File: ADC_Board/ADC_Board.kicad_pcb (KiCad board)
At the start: 2 copper layers, 93 x 57.7 mm, 60 parts, among them IC1 UCC12040DVE, IC2 ADS131M04QPWRQ1, IC7 ISO7762FDWR, J1 Conn_01x01_Pin, J2 Conn_01x01_Pin, J3 Conn_01x08_Pin, J4 Conn_01x01_Pin, J5 Conn_01x01_Pin, J6 Conn_01x08_Pin, U1 OPA990IDCKR, U2 OPA990IDCKR, U3 INA210AIDCKR, U4 INA210AIDCKR, U5 Nucleo_L432KC, U6 LM3940IMP-3.3

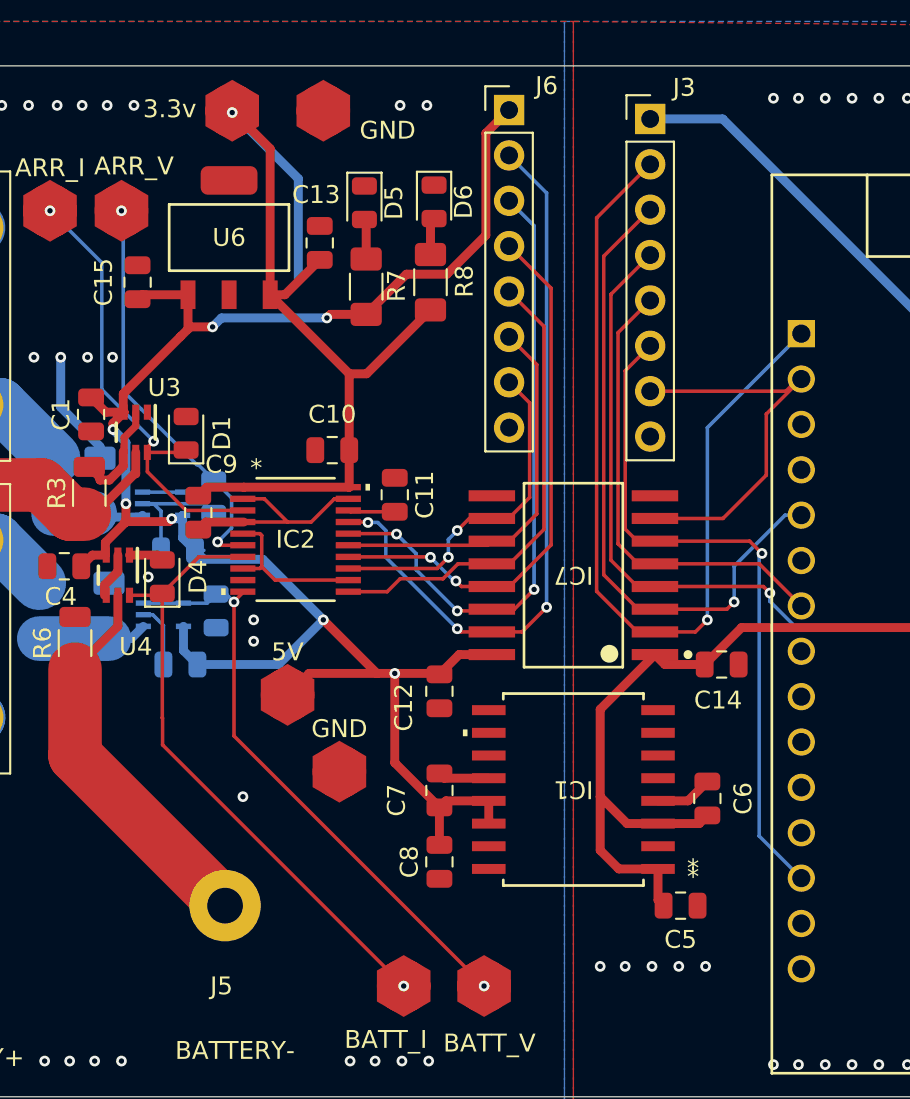
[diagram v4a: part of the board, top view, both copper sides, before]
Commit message: cleaned up some traces
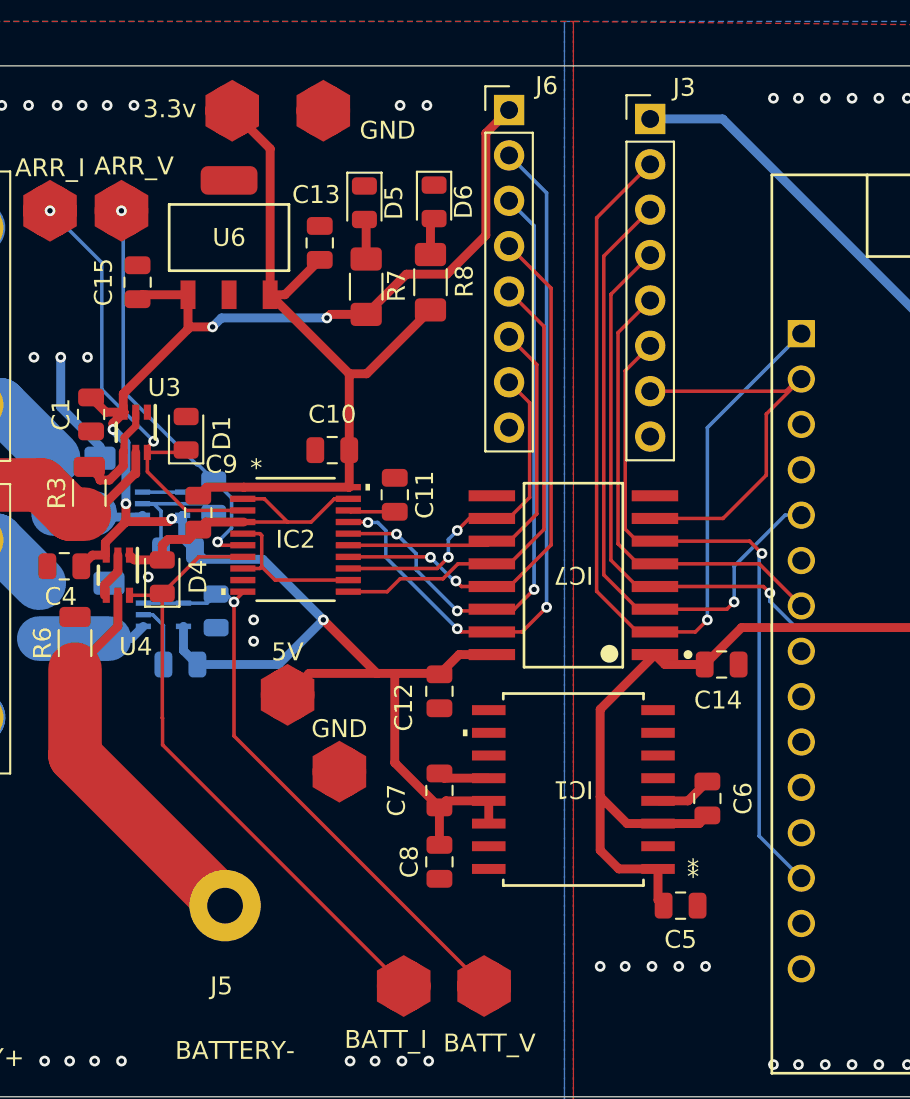
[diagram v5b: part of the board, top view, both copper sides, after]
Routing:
- net +3.3V: track 53.2 -> 42.1 mm, vias 1 -> 0
- net GND: track 52.5 -> 55.7 mm, vias 66 -> 64
- net +5V_I: track 92.6 -> 90.3 mm
- net +5V: track 108.0 -> 106.8 mm, vias 7 -> 6
- net /DRDY_I: track 22.8 -> 22.2 mm
- net /BATTERY_VOLTAGE+: vias 2 -> 1
- net /BATTERY_CURRENT+: vias 1 -> 0
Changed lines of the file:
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@@
+	)
+	(segment
+		(start 177.485004 76.144999)
+		(end 177.485004 75.314996)
+		(width 0.5)
+		(layer "F.Cu")
+		(net 1)
 	)
 	(segment
@@
 	)
 	(segment
+		(start 177.8 75)
+		(end 178.95 75)
+		(width 0.5)
+		(layer "F.Cu")
+		(net 1)
+	)
+	(segment
 		(start 193.105 84.555)
 		(end 193 84.45)
@@
 	)
 	(segment
-		(start 175.650001 75.875001)
-		(end 177.215006 75.875001)
-		(width 0.5)
-		(layer "F.Cu")
-		(net 1)
-	)
-	(segment
 		(start 175 76.800001)
 		(end 175 75.875001)
@@
 	)
 	(segment
+		(start 175.650001 75.875001)
+		(end 175.919999 76.144999)
+		(width 0.5)
+		(layer "F.Cu")
+		(net 1)
+	)
+	(segment
 		(start 175.3 70.9)
 		(end 175.3 70.075001)
@@
 		(end 187.95275 77.275002)
 		(width 0.2)
+		(layer "F.Cu")
+		(net 1)
+	)
+	(segment
+		(start 178.95 75)
+		(end 179.5 74.45)
+		(width 0.5)
 		(layer "F.Cu")
 		(net 1)
@@
 	)
 	(segment
-		(start 177.215006 75.875001)
-		(end 177.485004 76.144999)
-		(width 0.5)
-		(layer "F.Cu")
-		(net 1)
-	)
-	(segment
 		(start 175.350001 70.125002)
 		(end 175.350001 69.300002)
@@
 	)
 	(segment
+		(start 175.919999 76.144999)
+		(end 177.485004 76.144999)
+		(width 0.5)
+		(layer "F.Cu")
+		(net 1)
+	)
+	(segment
 		(start 182.04725 72.725001)
 		(end 183.2 72.725001)
@@
 		(net 1)
 	)
+	(segment
+		(start 177.485004 75.314996)
+		(end 177.8 75)
+		(width 0.5)
+		(layer "F.Cu")
+		(net 1)
+	)
 	(via
 		(at 175.9 50.7)
@@
 	)
 	(via
-		(at 174.7 64.8)
-		(size 0.6)
-		(drill 0.3)
-		(layers "F.Cu" "B.Cu")
-		(free yes)
-		(net 1)
-	)
-	(via
 		(at 189.4 104.2)
 		(size 0.6)
@@
 	(via
 		(at 147.6 74.3)
-		(size 0.6)
-		(drill 0.3)
-		(layers "F.Cu" "B.Cu")
-		(free yes)
-		(net 1)
-	)
-	(via
-		(at 182 89.4)
 		(size 0.6)
 		(drill 0.3)
@@
 	)
 	(segment
-		(start 196.4233 89.635)
-		(end 195.7629 89.635)
-		(width 0.2)
-		(layer "F.Cu")
-		(net 2)
-	)
-	(segment
 		(start 185.7 82.5)
 		(end 184.5 83.7)
@@
 	)
 	(segment
-		(start 190.5 82.5)
-		(end 190.55 82.55)
-		(width 0.2)
-		(layer "F.Cu")
-		(net 2)
-	)
-	(segment
 		(start 195.6 57.971878)
 		(end 195.6 52.26)
@@
 	)
 	(segment
-		(start 178.9248 63.2234)
-		(end 178.5093 63.6389)
+		(start 175.299999 66.848201)
+		(end 178.9248 63.2234)
 		(width 0.5)
 		(layer "F.Cu")
@@
 		(net 2)
 	)
-	(segment
-		(start 175.299999 66.848201)
-		(end 178.5093 63.6389)
-		(width 0.5)
-		(layer "F.Cu")
-		(net 2)
-	)
-	(via
-		(at 190.5 82.5)
-		(size 0.6)
-		(drill 0.3)
-		(layers "F.Cu" "B.Cu")
-		(net 2)
-	)
 	(via
 		(at 180.3 63.1)
@@
 	)
 	(segment
-		(start 179.3141 75.6117)
-		(end 179.8141 75.6117)
-		(width 0.2)
-		(layer "B.Cu")
-		(net 2)
-	)
-	(segment
 		(start 178.67235 81.22235)
 		(end 179.45 82)
@@
 	)
 	(segment
-		(start 204.075169 81.445)
-		(end 205.065495 81.445)
-		(width 0.2)
-		(layer "F.Cu")
-		(net 4)
-	)
-	(segment
 		(start 209.918 79.932)
 		(end 207.85 82)
@@
 	)
 	(segment
-		(start 205.2371 90.905)
-		(end 205.8975 90.905)
-		(width 0.2)
-		(layer "F.Cu")
-		(net 4)
-	)
-	(segment
-		(start 205.8975 93.445)
-		(end 205.2371 93.445)
-		(width 0.2)
-		(layer "F.Cu")
-		(net 4)
-	)
-	(segment
 		(start 229.6 72.2)
 		(end 228.5 71.1)
@@
 	)
 	(segment
-		(start 188.1845 69.7655)
-		(end 187.95 70)
-		(width 0.2)
-		(layer "F.Cu")
-		(net 5)
-	)
-	(segment
 		(start 187.95 72.072252)
 		(end 187.95275 72.075002)
@@
 		(net 5)
 	)
-	(via
-		(at 181.4 51.1)
-		(size 0.6)
-		(drill 0.3)
-		(layers "F.Cu" "B.Cu")
-		(net 5)
-	)
-	(segment
-		(start 185.1 54.8)
-		(end 181.4 51.1)
-		(width 0.5)
-		(layer "B.Cu")
-		(net 5)
-	)
-	(segment
-		(start 185.1 60.4)
-		(end 185.1 54.8)
-		(width 0.5)
-		(layer "B.Cu")
-		(net 5)
-	)
 	(segment
 		(start 188.027748 73.45)
@@
 	)
 	(segment
-		(start 176.3 67.7)
-		(end 175.3 66.7)
-		(width 0.2)
-		(layer "B.Cu")
-		(net 8)
-	)
-	(segment
-		(start 179.4101 70.8101)
-		(end 176.3 67.7)
+		(start 175.3 66.7)
+		(end 179.4101 70.8101)
 		(width 0.2)
 		(layer "B.Cu")
@@
 		(net 9)
 	)
-	(via
-		(at 195.5 100)
-		(size 0.6)
-		(drill 0.3)
-		(layers "F.Cu" "B.Cu")
-		(net 9)
-	)
 	(segment
 		(start 178.67235 78.564901)
@@
 		(net 10)
 	)
-	(via
-		(at 191 100)
-		(size 0.6)
-		(drill 0.3)
-		(layers "F.Cu" "B.Cu")
-		(net 10)
-	)
 	(segment
 		(start 187.95275 76.625001)
@@
 		(width 0.2)
 		(layer "F.Cu")
-		(net 19)
-	)
-	(segment
-		(start 213.26 66.620821)
-		(end 213.26 66.02)
-		(width 0.2)
-		(layer "F.Cu")
